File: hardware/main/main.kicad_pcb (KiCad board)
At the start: 2 copper layers, 44 parts, among them J101 Conn_01x02_Female, J102 Conn_01x02_Female, J103 Conn_01x02_Female, U101 LM324

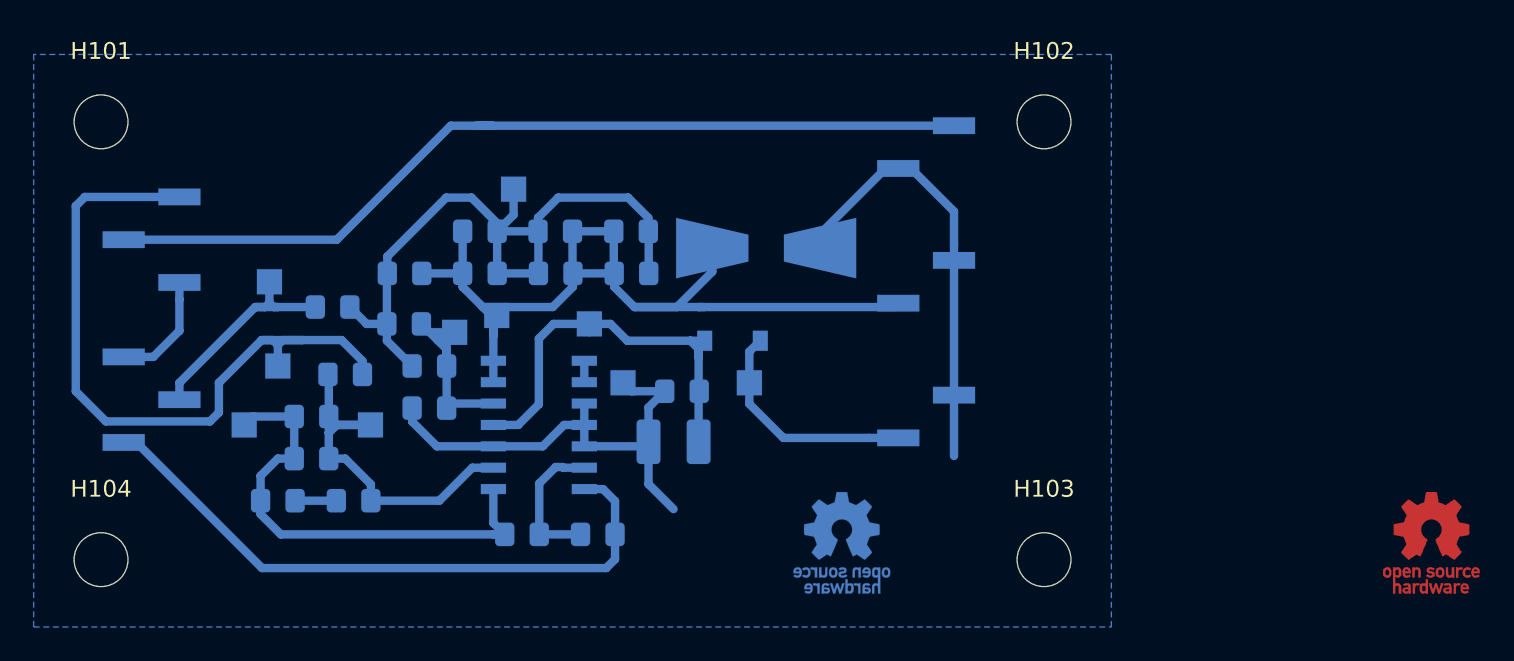
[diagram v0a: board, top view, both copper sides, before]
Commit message: PCB updated to single supply topology
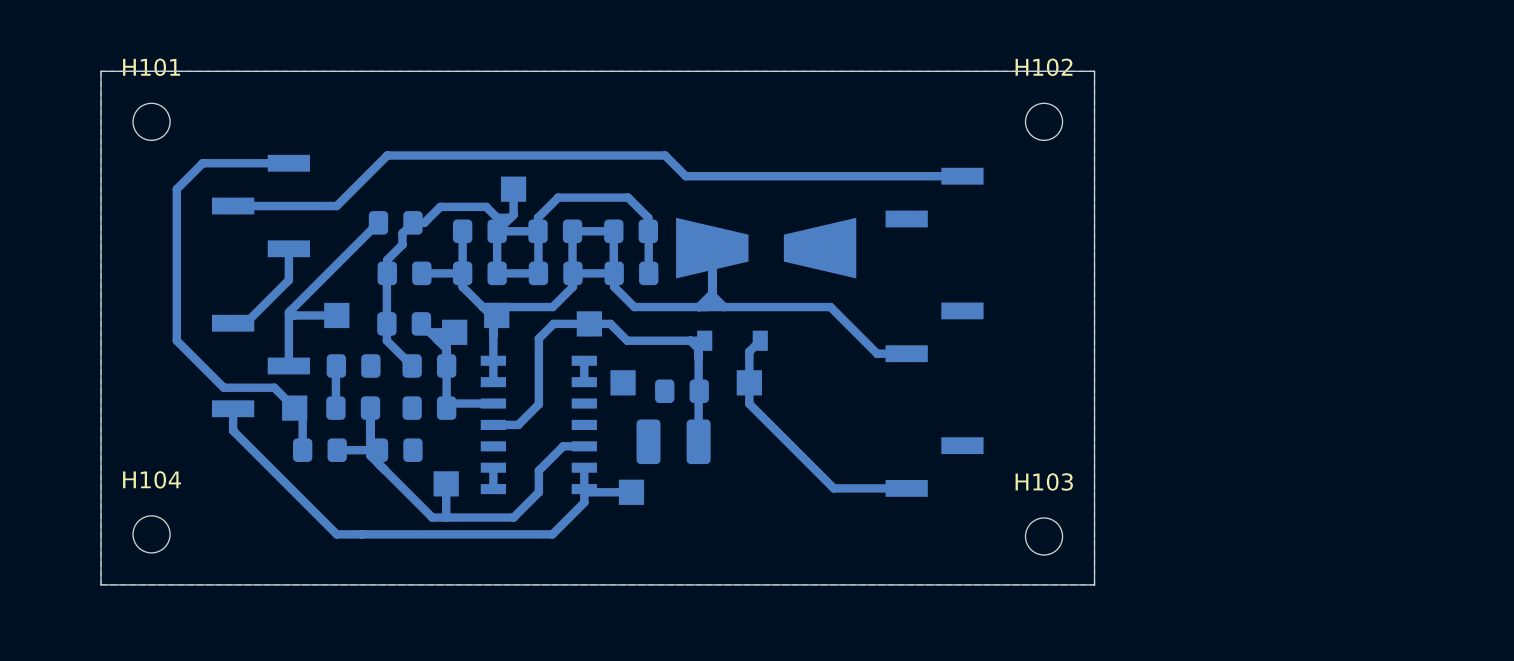
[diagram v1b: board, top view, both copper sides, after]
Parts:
- removed R102, R103, R104: 10k, Resistor_SMD:R_0805_2012Metric_Pad1.15x1.40mm_HandSolder
- removed REF** (x2): OSHW-Logo_5.7x6mm_Copper, Symbol:OSHW-Logo_5.7x6mm_Copper
- H101, H102, H103, H104: footprint MountingHole:MountingHole_3.2mm_M3 -> MountingHole:MountingHole_2.2mm_M2
- moved TP103 23.3 mm to (187.5, 77.0)
- moved C105 8.00 mm to (171.0, 69.5)
- moved C106 7.09 mm to (171.0, 72.0), turned to 180 degrees
- moved JP101 6.80 mm to (165.5, 60.0)
- moved JP102 6.80 mm to (165.5, 69.5)
- moved R105 6.25 mm to (173.5, 61.0)
- moved TP102 5.70 mm to (176.5, 76.5)
- moved C109 5.02 mm to (173.5, 74.5)
- moved TP104 4.47 mm to (170.0, 66.5)
- moved H104 3.35 mm to (159.0, 79.5)
- moved J101 3.04 mm to (205.5, 75.5)
- moved J102 3.04 mm to (205.5, 59.5)
- moved J103 3.04 mm to (205.5, 67.5)
- moved H101 3.00 mm to (159.0, 55.0)
- moved TP101 2.69 mm to (167.5, 72.0)
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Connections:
- C105 pad 2: Net-(C105-Pad2) -> GND
- C109 pad 2: Net-(C105-Pad2) -> GND
- R101 pad 2: Net-(C105-Pad2) -> Net-(JP101-Pad1)
- TP102 pad 1: Net-(C105-Pad2) -> Net-(C106-Pad1)
- TP103 pad 1: Net-(C106-Pad1) -> Net-(JP102-Pad1)
- U101 pad 1: Net-(C106-Pad1) -> Net-(U101-Pad1)
- U101 pad 12: GND -> Net-(C106-Pad1)
- U101 pad 13: Net-(R102-Pad2) -> Net-(JP102-Pad1)
- U101 pad 2: Net-(C105-Pad2) -> Net-(U101-Pad1)
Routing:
- net GND: track 55.3 -> 0.00 mm
- net Net-(C105-Pad2): track 22.6 -> 0.00 mm
- net Net-(JP101-Pad1): track 43.4 -> 27.6 mm
- net Net-(R102-Pad2): track 8.57 -> 0.00 mm
- net /INPUT: track 53.1 -> 45.1 mm
- net Net-(JP102-Pad1): track 38.1 -> 30.4 mm
- net /OUTPUT: track 56.2 -> 59.8 mm
- net Net-(D102-Pad2): track 14.2 -> 15.9 mm
- net Net-(C103-Pad2): track 42.8 -> 41.2 mm
- net Net-(U101-Pad1): track 0.00 -> 1.27 mm
- net Net-(C106-Pad1): track 28.3 -> 29.0 mm
- net Net-(JP101-Pad3): track 6.82 -> 6.23 mm
- net /MIDDLE: track 14.1 -> 13.6 mm
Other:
- board outline added: 59 x 30.5 mm

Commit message: ERC -> ok
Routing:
- net GND: track 0.00 -> 3.51 mm
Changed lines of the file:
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@@
     (thickness 1.6)
     (drawings 11)
-    (tracks 151)
+    (tracks 153)
     (zones 0)
     (modules 39)
@@
   (gr_line (start 242.5 32.5) (end 250 40) (layer B.SilkS) (width 0.12))
   (gr_line (start 242.5 32.5) (end 250 25) (layer B.SilkS) (width 0.12))
+  (segment (start 172.025 69.55) (end 174.475 72) (width 0.5) (layer B.Cu) (net 1))
+  (segment (start 172.025 69.5) (end 172.025 69.55) (width 0.5) (layer B.Cu) (net 1))
   (segment (start 184.7 74.27) (end 184.7 74.3) (width 0.5) (layer B.Cu) (net 6) (status 30))
   (segment (start 191.4875 74) (end 191.4875 68.9875) (width 0.5) (layer B.Cu) (net 2) (status 10))
